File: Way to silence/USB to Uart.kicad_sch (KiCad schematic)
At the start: 12 parts, among them Q1 BC817, Q2 BC817, U5 USB-TYPE-C-018

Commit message: [ADD] Shematics files settings
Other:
- title: (none) -> USB to UART
- moved on the sheet: C3, C4, R6, R7, R8, U5

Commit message: [ERC] 1 Warning cleaned
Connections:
- net +5V: no longer U5.A9 (VBUS), U5.B9 (VBUS)
- new net USB +5V: U5.A9 (VBUS), U5.B9 (VBUS)
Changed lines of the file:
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@@
     (effects (font (size 1.27 1.27)) (justify right bottom))
   )
-  (label "USB +5V" (at 147.32 40.64 180) (fields_autoplaced)
+  (label "+5V" (at 147.32 40.64 180) (fields_autoplaced)
     (effects (font (size 1.27 1.27)) (justify right bottom))
   )
-  (label "USB +5V" (at 165.1 53.34 0) (fields_autoplaced)
+  (label "+5V" (at 165.1 53.34 0) (fields_autoplaced)
     (effects (font (size 1.27 1.27)) (justify left bottom))
   )
@@
     (effects (font (size 1.27 1.27)) (justify right bottom))
   )
-  (label "USB +5V" (at 35.56 27.94 0) (fields_autoplaced)
+  (label "+5V" (at 35.56 27.94 0) (fields_autoplaced)
     (effects (font (size 1.27 1.27)) (justify left bottom))
   )
@@
     (effects (font (size 1.27 1.27)) (justify left bottom))
   )
-  (label "USB +5V" (at 54.61 91.44 180) (fields_autoplaced)
+  (label "+5V" (at 54.61 91.44 180) (fields_autoplaced)
     (effects (font (size 1.27 1.27)) (justify right bottom))
   )

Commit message: [FIX] Error in shematics
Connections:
- net USB +5V is gone; now on net +5V: U5.A9 (VBUS), U5.B9 (VBUS)
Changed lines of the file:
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@@
     (effects (font (size 1.27 1.27)) (justify left bottom))
   )
-  (label "USB +5V" (at 147.32 53.34 180) (fields_autoplaced)
+  (label "+5V" (at 147.32 53.34 180) (fields_autoplaced)
     (effects (font (size 1.27 1.27)) (justify right bottom))
   )
@@
     (effects (font (size 1.27 1.27)) (justify left bottom))
   )
-  (label "USB +5V" (at 165.1 40.64 0) (fields_autoplaced)
+  (label "+5V" (at 165.1 40.64 0) (fields_autoplaced)
     (effects (font (size 1.27 1.27)) (justify left bottom))
   )

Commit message: [FIX] LCSC Parts property
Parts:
- C2, C3: LCSC (none) -> C14663; LSCS C14663 -> (none)
- C4: LCSC (none) -> C19666; LSCS C19666 -> (none)
- R10, R9: LCSC (none) -> C25804; LSCS C25804 -> (none)
- R6, R7: LCSC (none) -> C425414; LSCS C425414 -> (none)
- R8: LCSC (none) -> C22935; LSCS C22935 -> (none)
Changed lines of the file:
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@@
       (effects (font (size 1.27 1.27)) hide)
     )
-    (property "LSCS" "C22935" (at 163.83 24.13 0)
+    (property "LCSC" "C22935" (at 163.83 24.13 0)
       (effects (font (size 1.27 1.27)) hide)
     )
@@
       (effects (font (size 1.27 1.27)) hide)
     )
-    (property "LSCS" "C25804" (at 78.74 22.86 0)
+    (property "LCSC" "C25804" (at 78.74 22.86 0)
       (effects (font (size 1.27 1.27)) hide)
     )
@@
       (effects (font (size 1.27 1.27)) hide)
     )
-    (property "LSCS" "C425414" (at 177.8 50.8 0)
+    (property "LCSC" "C425414" (at 177.8 50.8 0)
       (effects (font (size 1.27 1.27)) hide)
     )
@@
       (effects (font (size 1.27 1.27)) hide)
     )
-    (property "LSCS" "C19666" (at 72.39 95.25 90)
+    (property "LCSC" "C19666" (at 72.39 95.25 90)
       (effects (font (size 1.27 1.27)) hide)
     )
@@
       (effects (font (size 1.27 1.27)) hide)
     )
-    (property "LSCS" "C14663" (at 58.42 95.25 90)
+    (property "LCSC" "C14663" (at 58.42 95.25 90)
       (effects (font (size 1.27 1.27)) hide)
     )
@@
       (effects (font (size 1.27 1.27)) hide)
     )
-    (property "LSCS" "C425414" (at 134.62 43.18 0)
+    (property "LCSC" "C425414" (at 134.62 43.18 0)
       (effects (font (size 1.27 1.27)) hide)
     )
@@
       (effects (font (size 1.27 1.27)) hide)
     )
-    (property "LSCS" "C25804" (at 78.74 38.1 0)
+    (property "LCSC" "C25804" (at 78.74 38.1 0)
       (effects (font (size 1.27 1.27)) hide)
     )
@@
       (effects (font (size 1.27 1.27)) hide)
     )
-    (property "LSCS" "C14663" (at 63.5 87.63 0)
-      (effects (font (size 1.27 1.27)) hide)
-    )
+    (property "LCSC" "C14663" (at 63.5 87.63 0)
+      (effects (font (size 1.27 1.27)) hide)
+    )

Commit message: [ADD] U6 Q1 Q2 Rotations
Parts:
- Q1, Q2: JLCPCB Rotation Offset (none) -> 180
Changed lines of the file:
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@@
       (effects (font (size 1.27 1.27)) hide)
+    )
+    (property "JLCPCB Rotation Offset" "180" (at 59.69 19.05 0)
+      (effects (font (size 1.27 1.27)) (justify left) hide)
     )
     (pin "1")
@@
       (effects (font (size 1.27 1.27)) hide)
     )
-    (pin "1")
+    (property "JLCPCB Rotation Offset" "180" (at 59.69 41.91 0)
+      (effects (font (size 1.27 1.27)) (justify left) hide)
+    )
+    (pin "1")

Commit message: [ADD] First design fixes
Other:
- note added: "RX vers TX au lieu de RX vers RX TX vers RX au lieu de TX vers TX"
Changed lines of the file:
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@@
     (stroke (width 0) (type default))
+  )
+  (arc (start 63.5 46.99) (mid 73.5511 44.3146) (end 82.55 49.53)
+    (stroke (width 0) (type default))
+    (fill (type none))
+  )
+  (arc (start 69.85 48.26) (mid 69.324 46.99) (end 69.85 45.72)
+    (stroke (width 0) (type default))
+    (fill (type none))
+  )
+  (arc (start 74.93 46.99) (mid 68.4711 51.1533) (end 60.96 49.53)
+    (stroke (width 0) (type default))
+    (fill (type none))
+  )
+  (arc (start 66.04 50.8) (mid 65.514 49.53) (end 66.04 48.26)
+    (stroke (width 0) (type default))
+    (fill (type none))
+  )
+  (text "RX vers TX au lieu de RX vers RX\nTX vers RX au lieu de TX vers TX"
+    (at 45.72 57.15 0)
+    (effects (font (size 1.27 1.27) (color 255 0 34 1)) (justify left bottom))
   )
   (label "SH" (at 152.4 24.13 0) (fields_autoplaced)

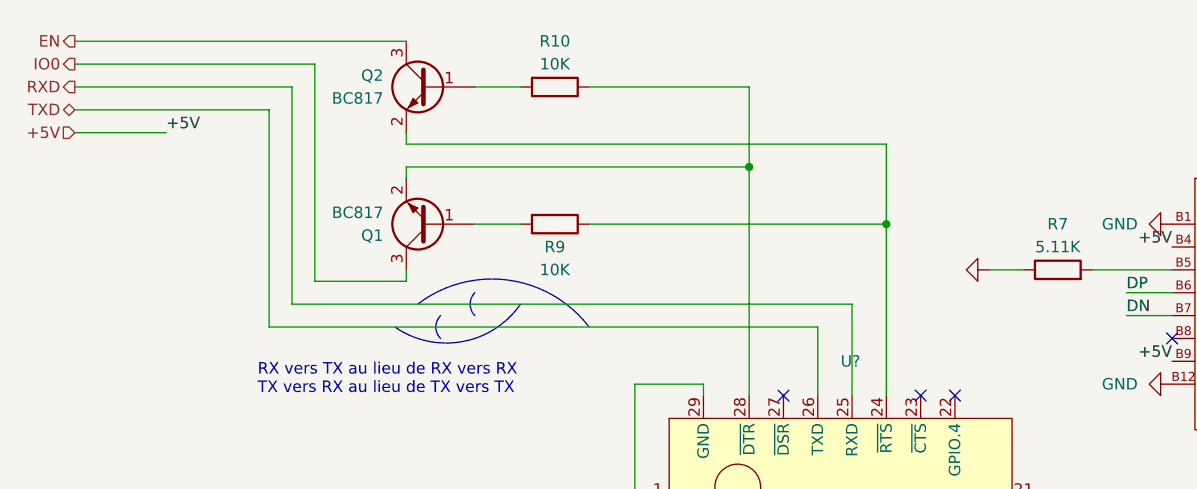
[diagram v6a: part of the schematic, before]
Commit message: [ADD] Notes to update design
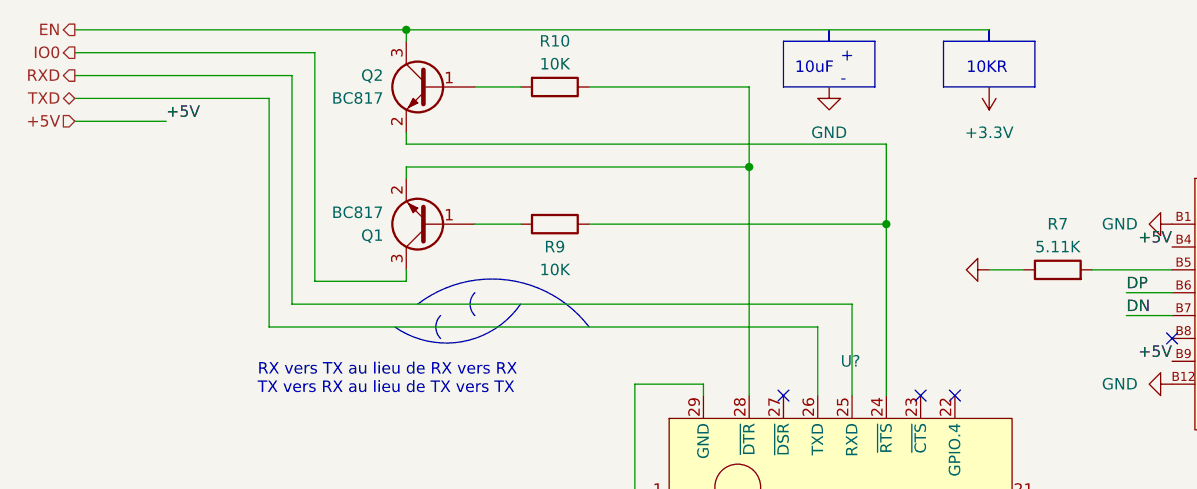
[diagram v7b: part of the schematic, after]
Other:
- note added: "+"
- note added: "-"
- note added: "10KR"
- note added: "10uF"
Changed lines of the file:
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@@
   (junction (at 115.57 38.1) (diameter 0) (color 0 0 0 0)
+  )
+  (junction (at 62.23 16.51) (diameter 0) (color 0 0 0 0)
   )
   (junction (at 72.39 91.44) (diameter 0) (color 0 0 0 0)
@@
     (stroke (width 0) (type default))
   )
-  (wire (pts (xy 52.07 44.45) (xy 52.07 20.32))
+  (wire (pts (xy 52.07 19.05) (xy 52.07 44.45))
     (stroke (width 0) (type default))
   )
@@
     (stroke (width 0) (type default))
   )
-  (wire (pts (xy 49.53 46.99) (xy 49.53 22.86))
+  (wire (pts (xy 49.53 21.59) (xy 49.53 46.99))
     (stroke (width 0) (type default))
   )
@@
     (stroke (width 0) (type default))
   )
+  (wire (pts (xy 62.23 16.51) (xy 62.23 17.78))
+    (stroke (width 0) (type default))
+  )
   (wire (pts (xy 115.57 29.21) (xy 62.23 29.21))
     (stroke (width 0) (type default))
@@
     (stroke (width 0) (type default))
   )
-  (wire (pts (xy 25.4 27.94) (xy 35.56 27.94))
+  (wire (pts (xy 25.4 26.67) (xy 35.56 26.67))
     (stroke (width 0) (type default))
   )
@@
     (stroke (width 0) (type default))
   )
-  (wire (pts (xy 46.99 49.53) (xy 46.99 25.4))
+  (wire (pts (xy 62.23 16.51) (xy 127 16.51))
+    (stroke (width 0) (type default))
+  )
+  (wire (pts (xy 46.99 24.13) (xy 46.99 49.53))
     (stroke (width 0) (type default))
   )
@@
     (stroke (width 0) (type default))
   )
-  (wire (pts (xy 49.53 22.86) (xy 25.4 22.86))
+  (wire (pts (xy 49.53 21.59) (xy 25.4 21.59))
     (stroke (width 0) (type default))
   )
@@
     (stroke (width 0) (type default))
   )
-  (wire (pts (xy 25.4 17.78) (xy 62.23 17.78))
-    (stroke (width 0) (type default))
-  )
-  (wire (pts (xy 52.07 20.32) (xy 25.4 20.32))
-    (stroke (width 0) (type default))
-  )
-  (wire (pts (xy 46.99 25.4) (xy 25.4 25.4))
+  (wire (pts (xy 25.4 16.51) (xy 62.23 16.51))
+    (stroke (width 0) (type default))
+  )
+  (wire (pts (xy 52.07 19.05) (xy 25.4 19.05))
+    (stroke (width 0) (type default))
+  )
+  (wire (pts (xy 46.99 24.13) (xy 25.4 24.13))
     (stroke (width 0) (type default))
   )
@@
     (stroke (width 0) (type default))
   )
+  (rectangle (start 121.92 17.78) (end 132.08 22.86)
+    (stroke (width 0) (type default))
+    (fill (type none))
+  )
   (arc (start 63.5 46.99) (mid 73.5511 44.3146) (end 82.55 49.53)
     (stroke (width 0) (type default))
     (fill (type none))
   )
+  (rectangle (start 109.22 16.51) (end 109.22 17.78)
+    (stroke (width 0) (type default))
+    (fill (type none))
+  )
   (arc (start 69.85 48.26) (mid 69.324 46.99) (end 69.85 45.72)
     (stroke (width 0) (type default))
@@
     (stroke (width 0) (type default))
     (fill (type none))
+  )
+  (rectangle (start 104.14 17.78) (end 114.3 22.86)
+    (stroke (width 0) (type default))
+    (fill (type none))
+  )
+  (rectangle (start 127 16.51) (end 127 17.78)
+    (stroke (width 0) (type default))
+    (fill (type none))
+  )
+  (text "10KR" (at 124.46 21.59 0)
+    (effects (font (size 1.27 1.27)) (justify left bottom))
+  )
+  (text "+" (at 110.49 20.32 0)
+    (effects (font (size 1.27 1.27)) (justify left bottom))
+  )
+  (text "10uF" (at 105.41 21.59 0)
+    (effects (font (size 1.27 1.27)) (justify left bottom))
   )
   (text "RX vers TX au lieu de RX vers RX\nTX vers RX au lieu de TX vers TX"
@@
     (effects (font (size 1.27 1.27) (color 255 0 34 1)) (justify left bottom))
   )
+  (text "-" (at 110.49 22.86 0)
+    (effects (font (size 1.27 1.27)) (justify left bottom))
+  )
   (label "SH" (at 152.4 24.13 0) (fields_autoplaced)
     (effects (font (size 1.27 1.27)) (justify left bottom))
@@
     (effects (font (size 1.27 1.27)) (justify right bottom))
   )
-  (label "+5V" (at 35.56 27.94 0) (fields_autoplaced)
+  (label "+5V" (at 35.56 26.67 0) (fields_autoplaced)
     (effects (font (size 1.27 1.27)) (justify left bottom))
   )
@@
     (effects (font (size 1.27 1.27)) (justify left bottom))
   )
-  (hierarchical_label "RXD" (shape output) (at 25.4 22.86 180) (fields_autoplaced)
+  (hierarchical_label "RXD" (shape output) (at 25.4 21.59 180) (fields_autoplaced)
     (effects (font (size 1.27 1.27)) (justify right))
   )
-  (hierarchical_label "TXD" (shape bidirectional) (at 25.4 25.4 180) (fields_autoplaced)
+  (hierarchical_label "TXD" (shape bidirectional) (at 25.4 24.13 180) (fields_autoplaced)
     (effects (font (size 1.27 1.27)) (justify right))
   )
-  (hierarchical_label "EN" (shape output) (at 25.4 17.78 180) (fields_autoplaced)
+  (hierarchical_label "EN" (shape output) (at 25.4 16.51 180) (fields_autoplaced)
     (effects (font (size 1.27 1.27)) (justify right))
   )
-  (hierarchical_label "IO0" (shape output) (at 25.4 20.32 180) (fields_autoplaced)
+  (hierarchical_label "IO0" (shape output) (at 25.4 19.05 180) (fields_autoplaced)
     (effects (font (size 1.27 1.27)) (justify right))
   )
-  (hierarchical_label "+5V" (shape input) (at 25.4 27.94 180) (fields_autoplaced)
+  (hierarchical_label "+5V" (shape input) (at 25.4 26.67 180) (fields_autoplaced)
     (effects (font (size 1.27 1.27)) (justify right))
   )
@@
         (path "/9822a1be-a034-44c3-8530-56368958b215/a2ee35dd-b0f9-4eed-a2dd-4bc114f32cf5"
           (reference "R10") (unit 1)
+        )
+      )
+    )
+  )
+  (symbol (lib_id "power:+3.3V") (at 127 22.86 180) (unit 1)
+    (in_bom yes) (on_board yes) (dnp no) (fields_autoplaced)
+    (property "Reference" "#PWR053" (at 127 19.05 0)
+      (effects (font (size 1.27 1.27)) hide)
+    )
+    (property "Value" "+3.3V" (at 127 27.94 0)
+      (effects (font (size 1.27 1.27)))
+    )
+    (property "Footprint" "" (at 127 22.86 0)
+      (effects (font (size 1.27 1.27)) hide)
+    )
+    (property "Datasheet" "" (at 127 22.86 0)
+      (effects (font (size 1.27 1.27)) hide)
+    )
+    (pin "1")
+    (instances
+      (project "Way to silence"
+        (path "/9822a1be-a034-44c3-8530-56368958b215/a2ee35dd-b0f9-4eed-a2dd-4bc114f32cf5"
+          (reference "#PWR053") (unit 1)
         )
       )
@@
         )
       )
+    )
+  )
+  (symbol (lib_id "power:GND") (at 109.22 22.86 0) (unit 1)
+    (in_bom yes) (on_board yes) (dnp no) (fields_autoplaced)
+    (property "Reference" "#PWR052" (at 109.22 29.21 0)
+      (effects (font (size 1.27 1.27)) hide)
+    )
+    (property "Value" "GND" (at 109.22 27.94 0)
+      (effects (font (size 1.27 1.27)))
+    )
+    (property "Footprint" "" (at 109.22 22.86 0)
+      (effects (font (size 1.27 1.27)) hide)
+    )
+    (property "Datasheet" "" (at 109.22 22.86 0)
+      (effects (font (size 1.27 1.27)) hide)
+    )
+    (pin "1")
+    (instances
+      (project "Way to silence"
+        (path "/9822a1be-a034-44c3-8530-56368958b215/a2ee35dd-b0f9-4eed-a2dd-4bc114f32cf5"
+          (reference "#PWR052") (unit 1)
+        )
+      )

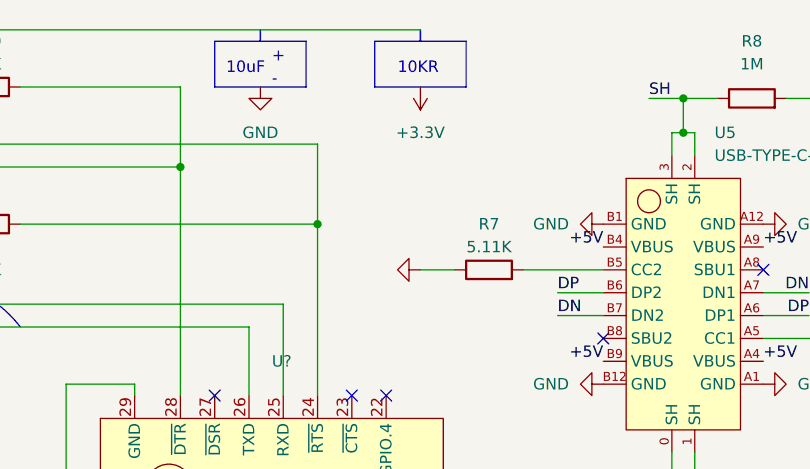
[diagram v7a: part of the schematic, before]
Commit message: [ADD] Notes to update design
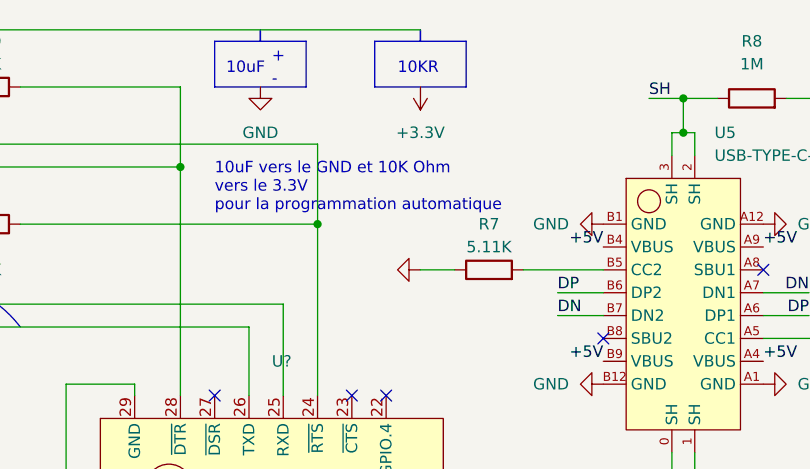
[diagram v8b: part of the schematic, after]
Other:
- note added: "10uF vers le GND et 10K Ohm vers le 3.3V pour la programmation automatique"
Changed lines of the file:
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@@
     (effects (font (size 1.27 1.27)) (justify left bottom))
+  )
+  (text "10uF vers le GND et 10K Ohm\nvers le 3.3V\npour la programmation automatique"
+    (at 104.14 36.83 0)
+    (effects (font (size 1.27 1.27) (color 241 0 0 1)) (justify left bottom))
   )
   (label "SH" (at 152.4 24.13 0) (fields_autoplaced)
